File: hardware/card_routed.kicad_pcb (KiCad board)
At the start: 2 copper layers, 143 x 80 mm, 1 part

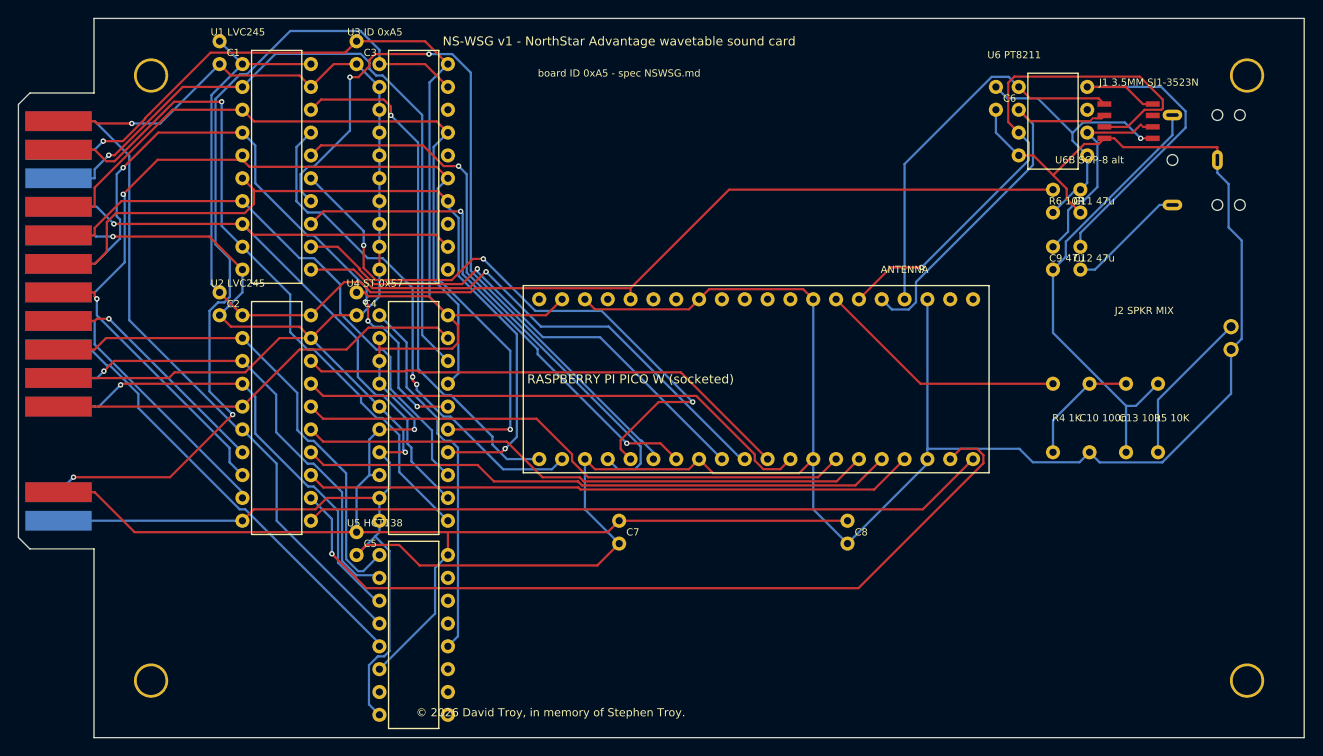
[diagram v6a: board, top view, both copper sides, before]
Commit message: Silkscreen tidy: zero collisions at full DRC severity
Root cause was gr_text center-anchoring vs left-anchored placement
assumptions. DIP references now run vertically inside their body
outlines (collision-proof), audio passives use short staggered refs
(values in the BOM), Pico label centered within its outline, memorial
line shifted clear of U5. Full-severity DRC is down from 13 findings
to just the benign embedded-footprint-library notice. Fab package and
plots regenerated.

Co-Authored-By: Claude Fable 5 <noreply@anthropic.com>
Claude-Session: https://claude.ai/code/session_01PB6zhL6oFB9zbtD4W85UDt
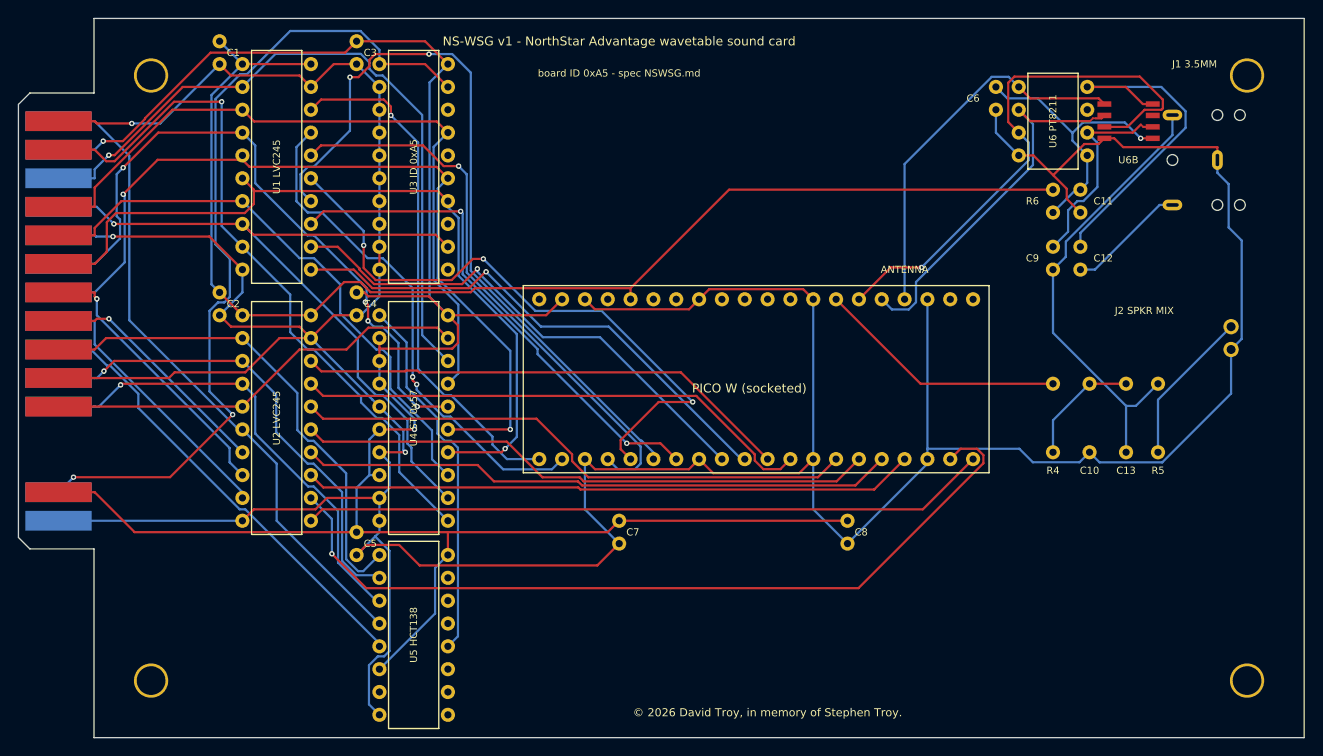
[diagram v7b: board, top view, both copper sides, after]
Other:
- board text added: "C10"
- board text added: "C11"
- board text added: "C12"
- board text added: "C13"
- board text added: "C9"
- board text added: "J1 3.5MM"
- board text added: "PICO W (socketed)"
- board text added: "R4"
- board text added: "R5"
- board text added: "R6"
- board text added: "U6B"
- board text removed: "C10 100n"
- board text removed: "C11 47u"
- board text removed: "C12 47u"
- board text removed: "C13 10u"
- board text removed: "C9 47u"
- board text removed: "J1 3.5MM SJ1-3523N"
- board text removed: "R4 1K"
- board text removed: "R5 10K"
- board text removed: "R6 10R"
- board text removed: "RASPBERRY PI PICO W (socketed)"
- board text removed: "U6B SOP-8 alt"
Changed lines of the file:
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@@
   (gr_line (start 0.0 8.2982) (end 0.0 0.0) (layer "Edge.Cuts") (width 0.1))
   (gr_rect (start 17.526 3.556) (end 23.114 29.464) (layer "F.SilkS") (width 0.15) (fill none))
-  (gr_text "U1 LVC245" (at 16.002 1.524) (layer "F.SilkS") (effects (font (size 0.8 0.8) (thickness 0.15))))
+  (gr_text "U1 LVC245" (at 20.32 16.51 90) (layer "F.SilkS") (effects (font (size 0.8 0.8) (thickness 0.15))))
   (gr_rect (start 17.526 31.496) (end 23.114 57.404) (layer "F.SilkS") (width 0.15) (fill none))
-  (gr_text "U2 LVC245" (at 16.002 29.464) (layer "F.SilkS") (effects (font (size 0.8 0.8) (thickness 0.15))))
+  (gr_text "U2 LVC245" (at 20.32 44.45 90) (layer "F.SilkS") (effects (font (size 0.8 0.8) (thickness 0.15))))
   (gr_rect (start 32.766 3.556) (end 38.354 29.464) (layer "F.SilkS") (width 0.15) (fill none))
-  (gr_text "U3 ID 0xA5" (at 31.242 1.524) (layer "F.SilkS") (effects (font (size 0.8 0.8) (thickness 0.15))))
+  (gr_text "U3 ID 0xA5" (at 35.56 16.51 90) (layer "F.SilkS") (effects (font (size 0.8 0.8) (thickness 0.15))))
   (gr_rect (start 32.766 31.496) (end 38.354 57.404) (layer "F.SilkS") (width 0.15) (fill none))
-  (gr_text "U4 ST 0x57" (at 31.242 29.464) (layer "F.SilkS") (effects (font (size 0.8 0.8) (thickness 0.15))))
+  (gr_text "U4 ST 0x57" (at 35.56 44.45 90) (layer "F.SilkS") (effects (font (size 0.8 0.8) (thickness 0.15))))
   (gr_rect (start 32.766 58.166) (end 38.354 78.994) (layer "F.SilkS") (width 0.15) (fill none))
-  (gr_text "U5 HCT138" (at 31.242 56.134) (layer "F.SilkS") (effects (font (size 0.8 0.8) (thickness 0.15))))
+  (gr_text "U5 HCT138" (at 35.56 68.58 90) (layer "F.SilkS") (effects (font (size 0.8 0.8) (thickness 0.15))))
   (gr_rect (start 103.886 6.096) (end 109.474 16.764) (layer "F.SilkS") (width 0.15) (fill none))
-  (gr_text "U6 PT8211" (at 102.362 4.064) (layer "F.SilkS") (effects (font (size 0.8 0.8) (thickness 0.15))))
-  (gr_text "U6B SOP-8 alt" (at 110.744 15.748) (layer "F.SilkS") (effects (font (size 0.8 0.8) (thickness 0.15))))
+  (gr_text "U6 PT8211" (at 106.68 11.43 90) (layer "F.SilkS") (effects (font (size 0.8 0.8) (thickness 0.15))))
+  (gr_text "U6B" (at 115.062 15.748) (layer "F.SilkS") (effects (font (size 0.8 0.8) (thickness 0.15))))
   (gr_rect (start 47.752 29.718) (end 99.568 50.546) (layer "F.SilkS") (width 0.15) (fill none))
-  (gr_text "RASPBERRY PI PICO W (socketed)" (at 59.69 40.132) (layer "F.SilkS") (effects (font (size 1.0 1.0) (thickness 0.15))))
+  (gr_text "PICO W (socketed)" (at 72.898 41.148) (layer "F.SilkS") (effects (font (size 1.0 1.0) (thickness 0.15))))
   (gr_text "ANTENNA" (at 90.17 27.94) (layer "F.SilkS") (effects (font (size 0.8 0.8) (thickness 0.15))))
   (zone (net 0) (net_name "") (layers "F.Cu" "B.Cu") (name "antenna-keepout") (hatch edge 0.508) (connect_pads (clearance 0)) (min_thickness 0.25) (keepout (tracks allowed) (vias not_allowed) (pads allowed) (copperpour not_allowed) (footprints allowed)) (fill (thermal_gap 0.5) (thermal_bridge_width 0.5)) (polygon (pts (xy 91.948 28.956) (xy 102.108 28.956) (xy 102.108 51.308) (xy 91.948 51.308))))
-  (gr_text "R6 10R" (at 108.204 20.32) (layer "F.SilkS") (effects (font (size 0.8 0.8) (thickness 0.15))))
-  (gr_text "C11 47u" (at 111.252 20.32) (layer "F.SilkS") (effects (font (size 0.8 0.8) (thickness 0.15))))
-  (gr_text "C9 47u" (at 108.204 26.67) (layer "F.SilkS") (effects (font (size 0.8 0.8) (thickness 0.15))))
-  (gr_text "C12 47u" (at 111.252 26.67) (layer "F.SilkS") (effects (font (size 0.8 0.8) (thickness 0.15))))
-  (gr_text "R4 1K" (at 108.204 44.45) (layer "F.SilkS") (effects (font (size 0.8 0.8) (thickness 0.15))))
-  (gr_text "C10 100n" (at 112.268 44.45) (layer "F.SilkS") (effects (font (size 0.8 0.8) (thickness 0.15))))
-  (gr_text "C13 10u" (at 116.332 44.45) (layer "F.SilkS") (effects (font (size 0.8 0.8) (thickness 0.15))))
-  (gr_text "R5 10K" (at 119.888 44.45) (layer "F.SilkS") (effects (font (size 0.8 0.8) (thickness 0.15))))
-  (gr_text "J1 3.5MM SJ1-3523N" (at 117.348 7.112) (layer "F.SilkS") (effects (font (size 0.8 0.8) (thickness 0.15))))
+  (gr_text "R6" (at 104.394 20.32) (layer "F.SilkS") (effects (font (size 0.8 0.8) (thickness 0.15))))
+  (gr_text "C11" (at 112.268 20.32) (layer "F.SilkS") (effects (font (size 0.8 0.8) (thickness 0.15))))
+  (gr_text "C9" (at 104.394 26.67) (layer "F.SilkS") (effects (font (size 0.8 0.8) (thickness 0.15))))
+  (gr_text "C12" (at 112.268 26.67) (layer "F.SilkS") (effects (font (size 0.8 0.8) (thickness 0.15))))
+  (gr_text "R4" (at 106.68 50.292) (layer "F.SilkS") (effects (font (size 0.8 0.8) (thickness 0.15))))
+  (gr_text "C10" (at 110.744 50.292) (layer "F.SilkS") (effects (font (size 0.8 0.8) (thickness 0.15))))
+  (gr_text "C13" (at 114.808 50.292) (layer "F.SilkS") (effects (font (size 0.8 0.8) (thickness 0.15))))
+  (gr_text "R5" (at 118.364 50.292) (layer "F.SilkS") (effects (font (size 0.8 0.8) (thickness 0.15))))
+  (gr_text "J1 3.5MM" (at 122.428 5.08) (layer "F.SilkS") (effects (font (size 0.8 0.8) (thickness 0.15))))
   (gr_text "J2 SPKR MIX" (at 116.84 32.512) (layer "F.SilkS") (effects (font (size 0.8 0.8) (thickness 0.15))))
   (gr_text "C1" (at 15.494 3.81) (layer "F.SilkS") (effects (font (size 0.8 0.8) (thickness 0.15))))
@@
   (gr_text "C4" (at 30.734 31.75) (layer "F.SilkS") (effects (font (size 0.8 0.8) (thickness 0.15))))
   (gr_text "C5" (at 30.734 58.42) (layer "F.SilkS") (effects (font (size 0.8 0.8) (thickness 0.15))))
-  (gr_text "C6" (at 101.854 8.89) (layer "F.SilkS") (effects (font (size 0.8 0.8) (thickness 0.15))))
+  (gr_text "C6" (at 97.79 8.89) (layer "F.SilkS") (effects (font (size 0.8 0.8) (thickness 0.15))))
   (gr_text "C7" (at 59.944 57.15) (layer "F.SilkS") (effects (font (size 0.8 0.8) (thickness 0.15))))
   (gr_text "C8" (at 85.344 57.15) (layer "F.SilkS") (effects (font (size 0.8 0.8) (thickness 0.15))))
   (gr_text "NS-WSG v1 - NorthStar Advantage wavetable sound card" (at 58.42 2.54) (layer "F.SilkS") (effects (font (size 1.0 1.0) (thickness 0.15))))
   (gr_text "board ID 0xA5 - spec NSWSG.md" (at 58.42 6.096) (layer "F.SilkS") (effects (font (size 0.8 0.8) (thickness 0.15))))
-  (gr_text "© 2026 David Troy, in memory of Stephen Troy." (at 50.8 77.216) (layer "F.SilkS") (effects (font (size 0.9 0.9) (thickness 0.15))))
+  (gr_text "© 2026 David Troy, in memory of Stephen Troy." (at 74.93 77.216) (layer "F.SilkS") (effects (font (size 0.9 0.9) (thickness 0.15))))
   (segment (start 29.21 5.08) (end 26.67 5.08) (width 0.25) (layer "F.Cu") (net 1))
   (segment (start 26.67 5.08) (end 24.13 7.62) (width 0.25) (layer "F.Cu") (net 1))
